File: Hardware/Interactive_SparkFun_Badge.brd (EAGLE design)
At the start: 88.9 x 63.5 mm, 30 parts, among them J1 AVR_SPI_PRG_6PTH, U1 ATMEGA328P

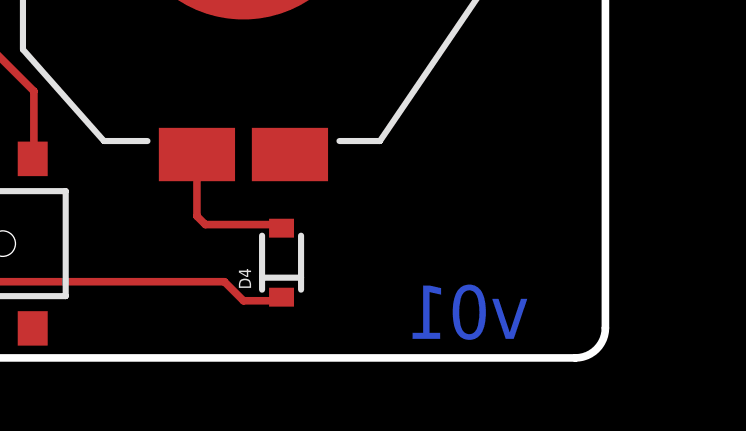
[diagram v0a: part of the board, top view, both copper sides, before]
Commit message: Fixing version number to v10
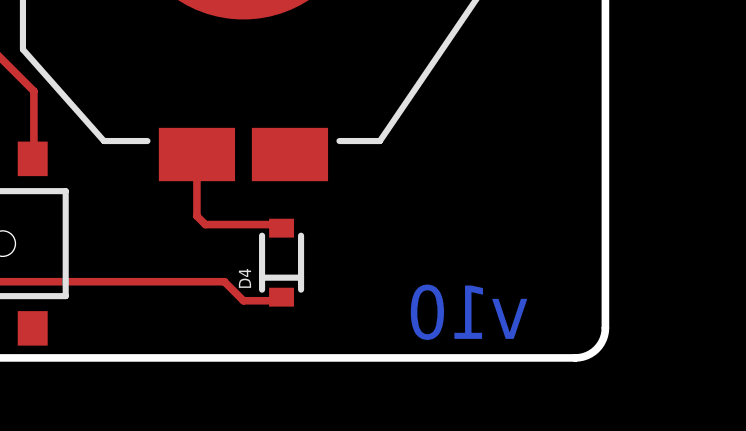
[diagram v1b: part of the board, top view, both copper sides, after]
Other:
- board text added: "v10"
- board text removed: "v01"
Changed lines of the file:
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@@
 <board>
 <plain>
-<text x="86.36" y="0.635" size="1.778" layer="16" font="vector" ratio="15" rot="MR0">v01</text>
+<text x="86.36" y="0.635" size="1.778" layer="16" font="vector" ratio="15" rot="MR0">v10</text>
 <text x="48.26" y="-8.89" size="1.778" layer="51" font="vector" ratio="15">Toni Klopfenstein</text>
 <text x="3.175" y="29.21" size="1.27" layer="21" font="vector" ratio="15" rot="SR270">3.3V FTDI</text>

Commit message: Switching to Schottky diode
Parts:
- D3, D4: value DIODE-ZENER3.3V -> PMEG4005EJ
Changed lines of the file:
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@@
 <element name="J1" library="SparkFun-Connectors" package="2X3" value="AVR_SPI_PRG_6PTH" x="85.09" y="40.64" rot="R270"/>
 <element name="U$3" library="ML8511" package="INITIALS" value="ALPHABET" x="60.325" y="43.815" rot="R180"/>
-<element name="D3" library="SparkFun-DiscreteSemi" package="SOD-323" value="DIODE-ZENER3.3V" x="9.525" y="22.86" rot="R180">
-<attribute name="PROD_ID" value="DIO-11284" x="9.525" y="22.86" size="1.778" layer="27" font="vector" ratio="15" rot="R180" display="off"/>
-<attribute name="VALUE" value="3.3V" x="9.525" y="22.86" size="1.778" layer="27" rot="R180" display="off"/>
+<element name="D3" library="SparkFun-DiscreteSemi" package="SOD-323" value="PMEG4005EJ" x="9.525" y="22.86" rot="R180">
+<attribute name="PROD_ID" value="DIO-10955" x="9.525" y="22.86" size="1.778" layer="27" font="vector" ratio="15" rot="R180" display="off"/>
+<attribute name="VALUE" value="PMEG4005EJ" x="9.525" y="22.86" size="1.778" layer="27" rot="R180" display="off"/>
 </element>
-<element name="D4" library="SparkFun-DiscreteSemi" package="SOD-323" value="DIODE-ZENER3.3V" x="78.105" y="3.175" rot="R90">
-<attribute name="PROD_ID" value="DIO-11284" x="78.105" y="3.175" size="1.778" layer="27" font="vector" ratio="15" rot="R90" display="off"/>
-<attribute name="VALUE" value="3.3V" x="78.105" y="3.175" size="1.778" layer="27" rot="R90" display="off"/>
+<element name="D4" library="SparkFun-DiscreteSemi" package="SOD-323" value="PMEG4005EJ" x="78.105" y="3.175" rot="R90">
+<attribute name="PROD_ID" value="DIO-10955" x="78.105" y="3.175" size="1.778" layer="27" font="vector" ratio="15" rot="R90" display="off"/>
+<attribute name="VALUE" value="PMEG4005EJ" x="78.105" y="3.175" size="1.778" layer="27" rot="R90" display="off"/>
 </element>
 <element name="C1" library="SparkFun-Capacitors" package="0603-CAP" value="0.1uF" x="9.525" y="30.48">
